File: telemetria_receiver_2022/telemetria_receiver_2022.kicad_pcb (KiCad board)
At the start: 4 copper layers, 100 x 75 mm, 58 parts, among them J1 Micro_SD_Card, J2 Conn_01x06_Male, J4 USB_B_Mini, J5 Sygnały, J6 Zasilanie+CAN, J7 Diagnostyka, SW1 SW_Push, U1 NRF24L01_Breakout, U16 ATA6561-GAQW-N, U2 DS3231M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

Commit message: added logos lib, fixed routing, impedance matching of spi and sdio, removed external RTC, PCB rearrangement
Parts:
- removed C12: 100nF, Capacitor_SMD:C_0603_1608Metric
- removed FB1: 100R@100MHz, Inductor_SMD:L_0603_1608Metric
- removed R1, R2: 4.7kR, Resistor_SMD:R_0603_1608Metric
- removed R3, R4: 10kR, Resistor_SMD:R_0603_1608Metric
- removed U2: DS3231M, Package_SO:SOIC-16W_7.5x10.3mm_P1.27mm
- added G***: LOGO, Logos_fix:SignatureBox25mm, F.Cu at (114.3, 85.9)
- added G***: LOGO, Logos_fix:PUTM_LOGO_18mm, F.Cu at (110.7, 73.7)
- U4: footprint Package_TO_SOT_SMD:SOT-223 -> Package_TO_SOT_SMD:SOT-223-3_TabPin2
- moved J2 54.4 mm to (168.5, 125.6), turned to 90 degrees
- moved R6 52.6 mm to (183.9, 122.0), turned to 90 degrees
- moved C11 51.5 mm to (185.4, 122.0), turned to 90 degrees
- moved SW1 49.3 mm to (188.5, 127.6)
- moved C7 24.1 mm to (187.2, 101.3)
- moved FB2 24.1 mm to (184.2, 101.3), turned to 0 degrees
- moved L1 8.69 mm to (140.0, 93.7)
- moved J1 7.87 mm to (177.0, 110.0)
- moved R56 5.34 mm to (125.2, 78.1), turned to 90 degrees
- moved BT1 3.42 mm to (171.7, 87.0)
- moved R11 2.29 mm to (130.0, 120.9)
- moved R12 2.29 mm to (127.8, 120.9)
- moved D7 1.53 mm to (170.0, 66.9)
- moved R5 1.51 mm to (158.1, 103.4)
- moved C1 0.57 mm to (126.0, 107.7)
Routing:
- net +3V3: track 257.7 -> 31.6 mm, vias 13 -> 26
- net GND: track 20.7 -> 124.7 mm, vias 30 -> 221
- net /SW_CLK: track 135.9 -> 34.2 mm, vias 0 -> 2
- net /SW_DIO: track 136.1 -> 40.0 mm, vias 2 -> 1
- net /+3V3_uC: track 84.5 -> 23.9 mm, vias 5 -> 9
- net /I2C1_SDA: track 27.3 -> 0.00 mm, vias 2 -> 0
- net /I2C1_SCL: track 25.3 -> 0.00 mm, vias 2 -> 0
- net /SD_card/+3V3_SD: track 37.5 -> 16.3 mm, vias 2 -> 0
- net /SDMMC1_D2: track 69.7 -> 50.1 mm, vias 2 -> 0
- net /SDMMC1_D3: track 64.8 -> 50.1 mm, vias 2 -> 0
- net /NRF24_CSN: track 32.6 -> 18.1 mm, vias 0 -> 1
- net +BATT: track 27.1 -> 12.8 mm
- net /SDMMC1_CMD: track 62.6 -> 50.0 mm, vias 2 -> 0
- net /NRF24_MOSI: track 37.2 -> 25.0 mm
- net /SDMMC1_D0: track 61.6 -> 50.2 mm, vias 2 -> 0
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- added copper zone on F.Cu, net +3V3
- added copper zone on In2.Cu, net +3V3
- added copper zone on F.Cu, net /+3V3_uC
- added copper zone on In2.Cu, net /+3V3_uC
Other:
- board text added: "Gleb Fedorovich"

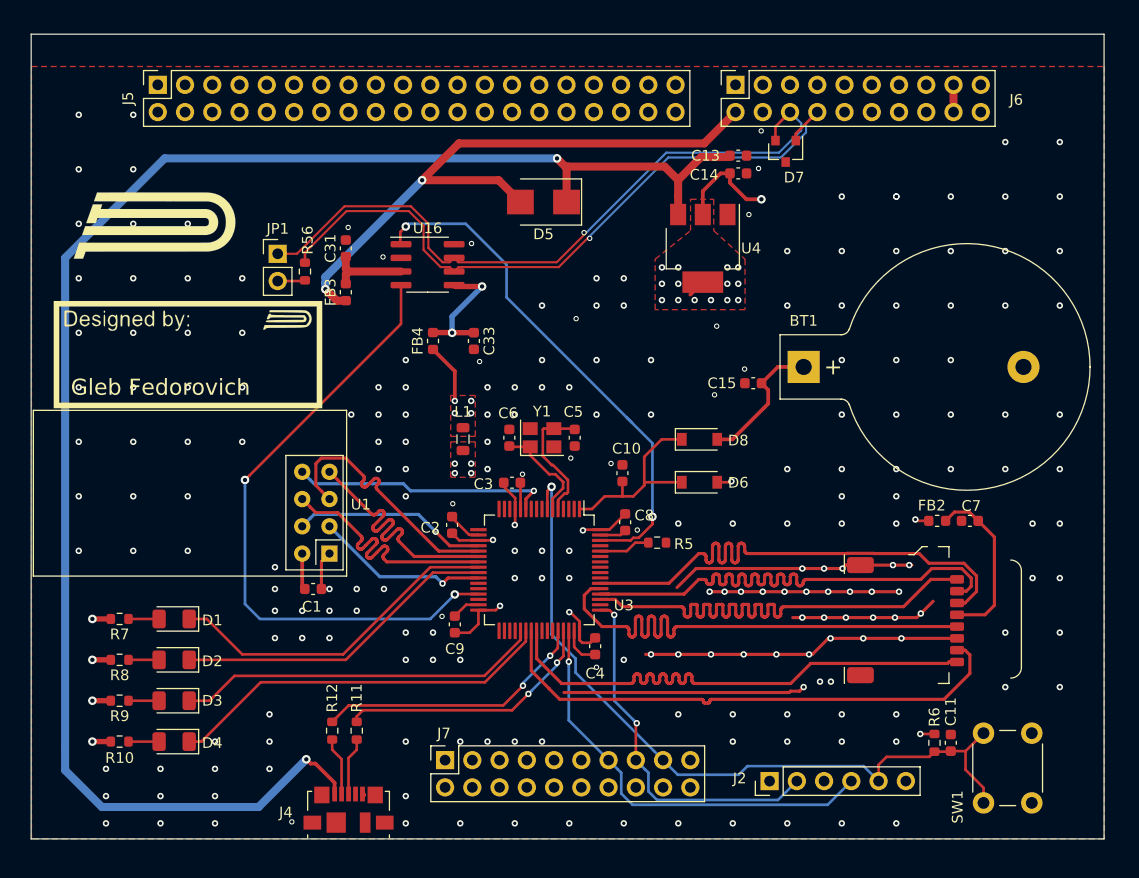
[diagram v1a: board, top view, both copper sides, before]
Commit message: controlled impedance tracks, added mounting holes
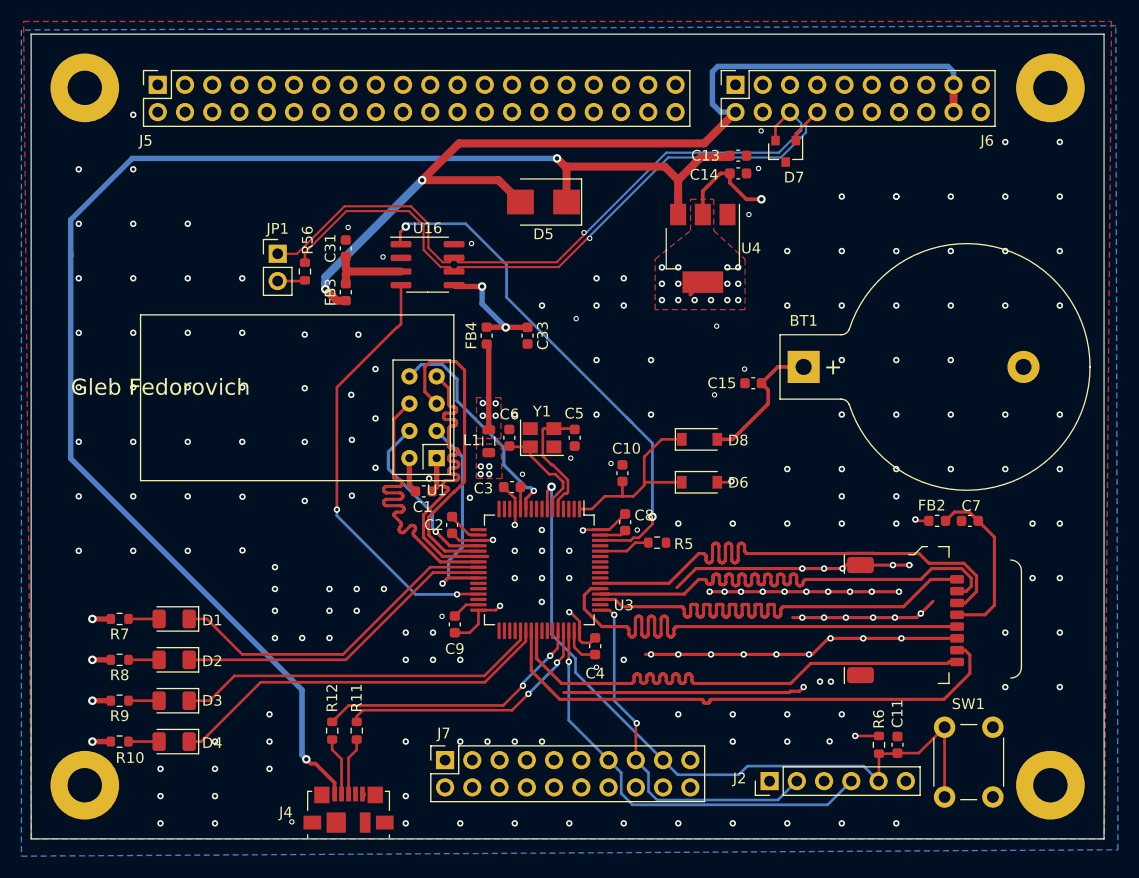
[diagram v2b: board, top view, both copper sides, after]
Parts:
- removed G***: LOGO, Logos_fix:SignatureBox25mm
- removed G***: LOGO, Logos_fix:PUTM_LOGO_18mm
- added H1: MountingHole, MountingHole:MountingHole_3.2mm_M3_Pad, F.Cu at (194.7, 61.0)
- added H2: MountingHole, MountingHole:MountingHole_3.2mm_M3_Pad, F.Cu at (194.7, 126.0)
- added H3: MountingHole, MountingHole:MountingHole_3.2mm_M3_Pad, F.Cu at (104.7, 61.0)
- added H4: MountingHole, MountingHole:MountingHole_3.2mm_M3_Pad, F.Cu at (104.7, 126.0)
- moved C1 13.8 mm to (136.3, 98.6)
- moved U1 13.4 mm to (137.5, 95.5)
- moved R6 5.18 mm to (178.7, 122.2)
- moved C33 5.02 mm to (146.0, 84.1)
- moved FB4 5.02 mm to (142.2, 84.1)
- moved C11 4.97 mm to (180.5, 122.2)
- moved SW1 3.67 mm to (184.8, 127.1)
- moved L1 2.41 mm to (142.4, 93.9)
- moved C3 0.41 mm to (144.5, 98.2)
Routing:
- net +5V: track 60.6 -> 90.2 mm
- net /CAN_RX: track 59.0 -> 40.2 mm
- net +5VD: track 152.5 -> 136.8 mm
- net /NRF24_MISO: track 25.0 -> 31.0 mm
- net /NRF24_SCK: track 25.0 -> 30.1 mm
- net /NRF24_MOSI: track 25.0 -> 30.1 mm
- net /NRF24_IRQ: track 24.3 -> 21.1 mm
- net +3V3: track 31.6 -> 34.9 mm
- net /NRF24_CE: track 16.3 -> 19.5 mm
- net /NRST: track 71.6 -> 69.8 mm
- net /NRF24_CSN: track 18.1 -> 16.6 mm
- net GND: track 124.7 -> 123.9 mm, vias 221 -> 210
- net /CAN/+3V3_VIO: track 12.0 -> 11.2 mm
- added copper zone on B.Cu, net GND

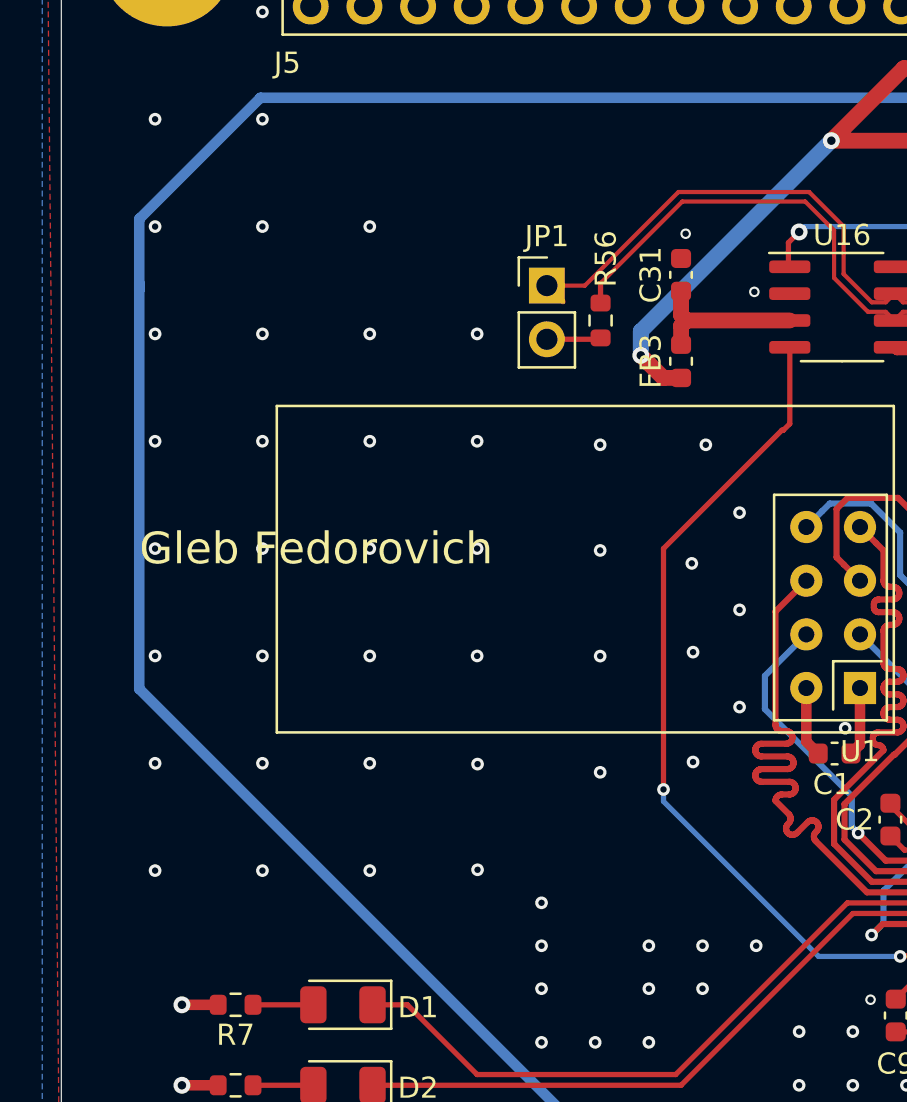
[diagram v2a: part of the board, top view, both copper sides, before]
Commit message: Added 3d model and logos
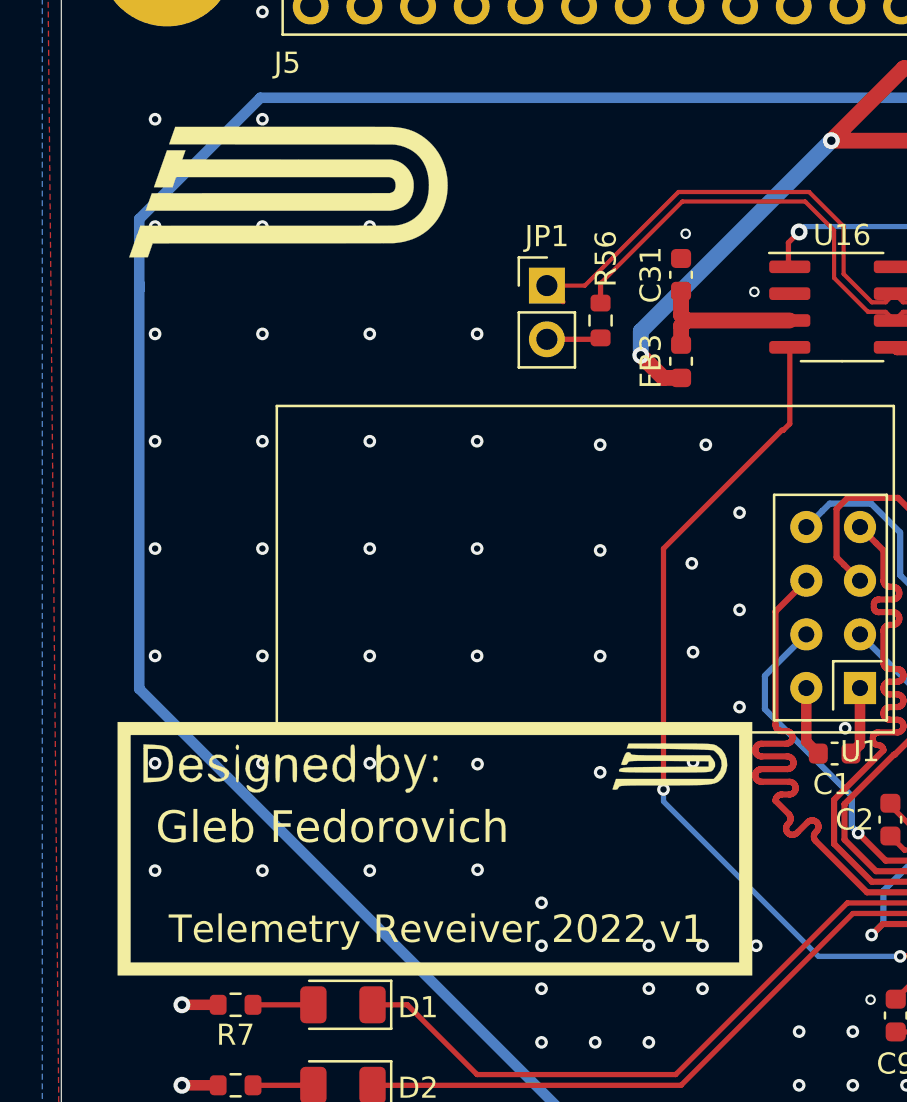
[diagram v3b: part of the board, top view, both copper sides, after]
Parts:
- added G***: LOGO, Logos_fix:SignatureBox30mm, F.Cu at (117.4, 103.1)
- added G***: LOGO, Logos_fix:PUTM_LOGO_18mm, F.Cu at (110.0, 71.9)
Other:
- board text added: "Telemetry Reveiver 2022 v1"

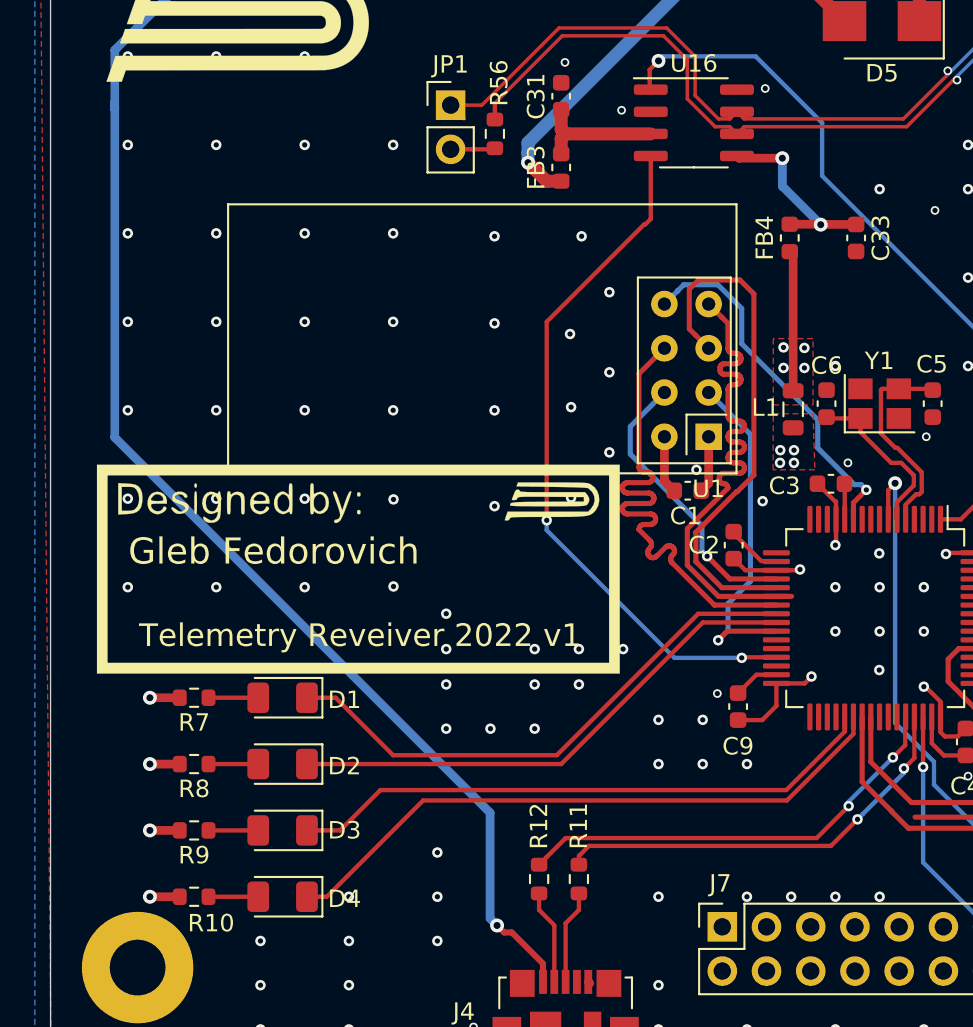
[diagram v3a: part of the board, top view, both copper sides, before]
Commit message: Transmiter placement changed
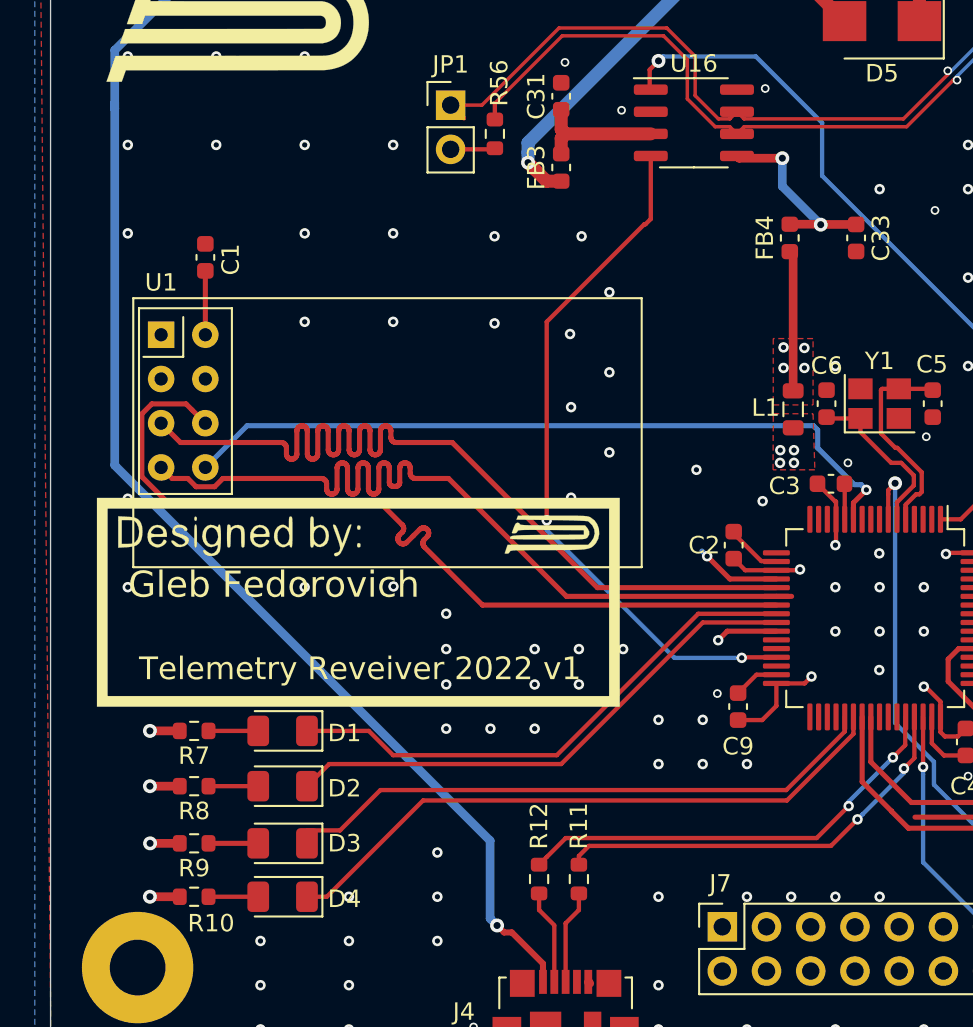
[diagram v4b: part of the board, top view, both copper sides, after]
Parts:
- moved U1 32.0 mm to (106.1, 89.6), turned to 0 degrees
- moved C1 30.8 mm to (108.6, 85.2), turned to 90 degrees
- moved D1 1.91 mm to (113.0, 112.4)
- moved G*** 1.91 mm to (117.4, 105.0)
- moved R7 1.91 mm to (108.0, 112.4)
- moved D2 1.27 mm to (113.0, 115.6)
- moved R8 1.27 mm to (108.0, 115.6)
- moved D3 0.74 mm to (113.0, 118.9)
- moved R9 0.74 mm to (108.0, 118.9)
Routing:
- net /NRF24_SCK: track 30.1 -> 54.4 mm
- net /NRF24_CE: track 19.5 -> 43.3 mm
- net /NRF24_CSN: track 16.6 -> 39.0 mm
- net /NRF24_IRQ: track 21.1 -> 43.1 mm
- net /NRF24_MOSI: track 30.1 -> 50.0 mm
- net /NRF24_MISO: track 31.0 -> 50.9 mm
- net GND: track 123.9 -> 120.7 mm, vias 210 -> 197
- net /LED_1: track 31.7 -> 30.9 mm
- net /LED_2: track 30.3 -> 30.9 mm
